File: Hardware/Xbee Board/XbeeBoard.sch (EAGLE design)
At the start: 2 parts

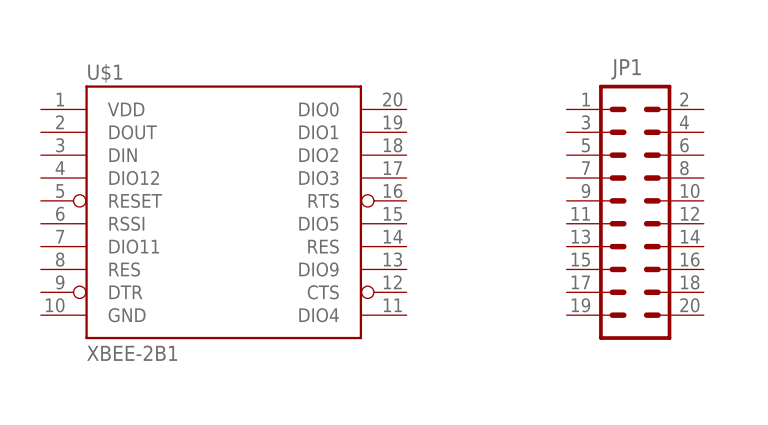
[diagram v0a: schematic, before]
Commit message: updated boards + logo 6 in illustrator
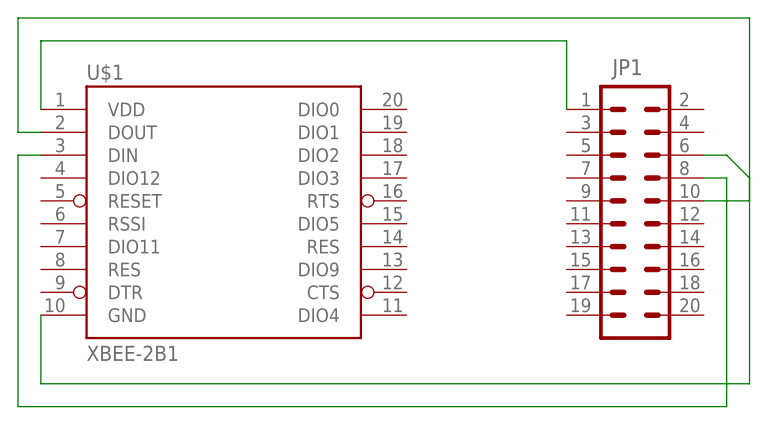
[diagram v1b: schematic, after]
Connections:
- new net N$1: JP1.1, U$1.VDD
- new net N$2: JP1.10, U$1.DOUT
- new net N$3: JP1.8, U$1.DIN
- new net N$4: JP1.6, U$1.GND
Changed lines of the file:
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@@
 <setting verticaltext="up"/>
 </settings>
-<grid distance="0.1" unitdist="inch" unit="inch" style="lines" multiple="1" display="no" altdistance="0.01" altunitdist="inch" altunit="inch"/>
+<grid distance="0.1" unitdist="inch" unit="inch" style="lines" multiple="1" display="yes" altdistance="0.01" altunitdist="inch" altunit="inch"/>
 <layers>
 <layer number="1" name="Top" color="4" fill="1" visible="no" active="no"/>
@@
 </busses>
 <nets>
+<net name="N$1" class="0">
+<segment>
+<pinref part="U$1" gate="G$1" pin="VDD"/>
+<wire x1="25.4" y1="68.58" x2="25.4" y2="76.2" width="0.1524" layer="91"/>
+<pinref part="JP1" gate="G$1" pin="1"/>
+<wire x1="25.4" y1="76.2" x2="83.82" y2="76.2" width="0.1524" layer="91"/>
+<wire x1="83.82" y1="76.2" x2="83.82" y2="68.58" width="0.1524" layer="91"/>
+</segment>
+</net>
+<net name="N$2" class="0">
+<segment>
+<pinref part="U$1" gate="G$1" pin="DOUT"/>
+<wire x1="25.4" y1="66.04" x2="22.86" y2="66.04" width="0.1524" layer="91"/>
+<wire x1="22.86" y1="66.04" x2="22.86" y2="78.74" width="0.1524" layer="91"/>
+<wire x1="22.86" y1="78.74" x2="104.14" y2="78.74" width="0.1524" layer="91"/>
+<wire x1="104.14" y1="78.74" x2="104.14" y2="58.42" width="0.1524" layer="91"/>
+<pinref part="JP1" gate="G$1" pin="10"/>
+<wire x1="104.14" y1="58.42" x2="99.06" y2="58.42" width="0.1524" layer="91"/>
+</segment>
+</net>
+<net name="N$3" class="0">
+<segment>
+<pinref part="U$1" gate="G$1" pin="DIN"/>
+<wire x1="25.4" y1="63.5" x2="22.86" y2="63.5" width="0.1524" layer="91"/>
+<wire x1="22.86" y1="63.5" x2="22.86" y2="35.56" width="0.1524" layer="91"/>
+<wire x1="22.86" y1="35.56" x2="101.6" y2="35.56" width="0.1524" layer="91"/>
+<wire x1="101.6" y1="35.56" x2="101.6" y2="60.96" width="0.1524" layer="91"/>
+<pinref part="JP1" gate="G$1" pin="8"/>
+<wire x1="101.6" y1="60.96" x2="99.06" y2="60.96" width="0.1524" layer="91"/>
+</segment>
+</net>
+<net name="N$4" class="0">
+<segment>
+<pinref part="U$1" gate="G$1" pin="GND"/>
+<wire x1="25.4" y1="45.72" x2="25.4" y2="38.1" width="0.1524" layer="91"/>
+<wire x1="25.4" y1="38.1" x2="104.14" y2="38.1" width="0.1524" layer="91"/>
+<wire x1="104.14" y1="38.1" x2="104.14" y2="60.96" width="0.1524" layer="91"/>
+<wire x1="104.14" y1="60.96" x2="101.6" y2="63.5" width="0.1524" layer="91"/>
+<pinref part="JP1" gate="G$1" pin="6"/>
+<wire x1="101.6" y1="63.5" x2="99.06" y2="63.5" width="0.1524" layer="91"/>
+</segment>
+</net>
 </nets>
 </sheet>
